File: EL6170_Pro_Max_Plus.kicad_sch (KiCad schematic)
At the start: 232 parts, among them CN1 PJ-327A0-SMT, J1 USB_C_Receptacle, J2 microSD, Q1 MMBT3904, Q2 MMBT3904, Q3 2N7002, Q4 AO3401A, Q5 AO3401A, SW1 SW_LEFT, SW10 SW_K4, SW11 SW_K5, SW12 SW_K6, SW13 SW_K7, SW14 SW_K8, SW15 SW_K9, SW16 SW_K0, SW17 SW_KQ, SW18 SW_KW, SW19 SW_KE, SW2 SW_UP, SW20 SW_KR, SW21 SW_KT, SW22 SW_KY, SW23 SW_KU, SW24 SW_KI, SW25 SW_KO, SW26 SW_KP, SW27 SW_KA, SW28 SW_KS, SW29 SW_KD, SW3 SW_DOWN, SW30 SW_KF, SW31 SW_KG, SW32 SW_KH, SW33 SW_KJ, SW34 SW_KK, SW35 SW_KL, SW36 SW_KZ, SW37 SW_KX, SW38 SW_KC, SW39 SW_KV, SW4 SW_RIGHT, SW40 SW_KB, SW41 SW_KN, SW42 SW_KM, SW43 SW_KCOM, SW44 SW_KDOT, SW45 SW_SHIFT, SW46 SW_CE(IO0), SW47 SW_OFF, SW48 SW_SECRET, SW49 SW_MCK, SW5 SW_UP2, SW50 SW_SPACE, SW51 SW_REMARK, SW52 SW_CALENDAR, SW53 SW_MODE, SW54 SW_ENTER, SW6 SW_DOWN2, SW7 SW_K1, SW8 SW_K2, SW9 SW_K3, U1 ESP32-S3, U10 ME6211C33M5, U11 TP5400_C2891434, U12 PCF8575DBR, U2 TPS61040DBV, U3 ESP-PSRAM64H, U4 W25Q128JVS, U5 ME6217C33M5, U6 CH340K, U7 RFANT5220110A0T, U8 CH334R, U9 PCM5102A, X1 40MHz, X2 12MHz

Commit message: PCB layout
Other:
- company: (none) -> libchara-dev
- title: (none) -> ProjectEL6170Pro
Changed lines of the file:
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@@
 	(generator_version "8.0")
 	(paper "A3")
+	(title_block
+		(title "ProjectEL6170Pro")
+		(date "2024-09-27")
+		(rev "2024-09-27")
+		(company "libchara-dev")
+		(comment 1 "EL6170 Pro Max Plus")
+	)
 	(junction
 		(at 245.11 199.39)

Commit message: sync
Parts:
- added R36: 10k, SparkFun-Resistor:R_0402_1005Metric, symbol SparkFun-Resistor:10k_0402
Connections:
- net STDBY is gone; now on net GPIO2: U11.4 (~{STDBY})
- net +3V3: now also R36.1
- net GPIO2: now also R36.2

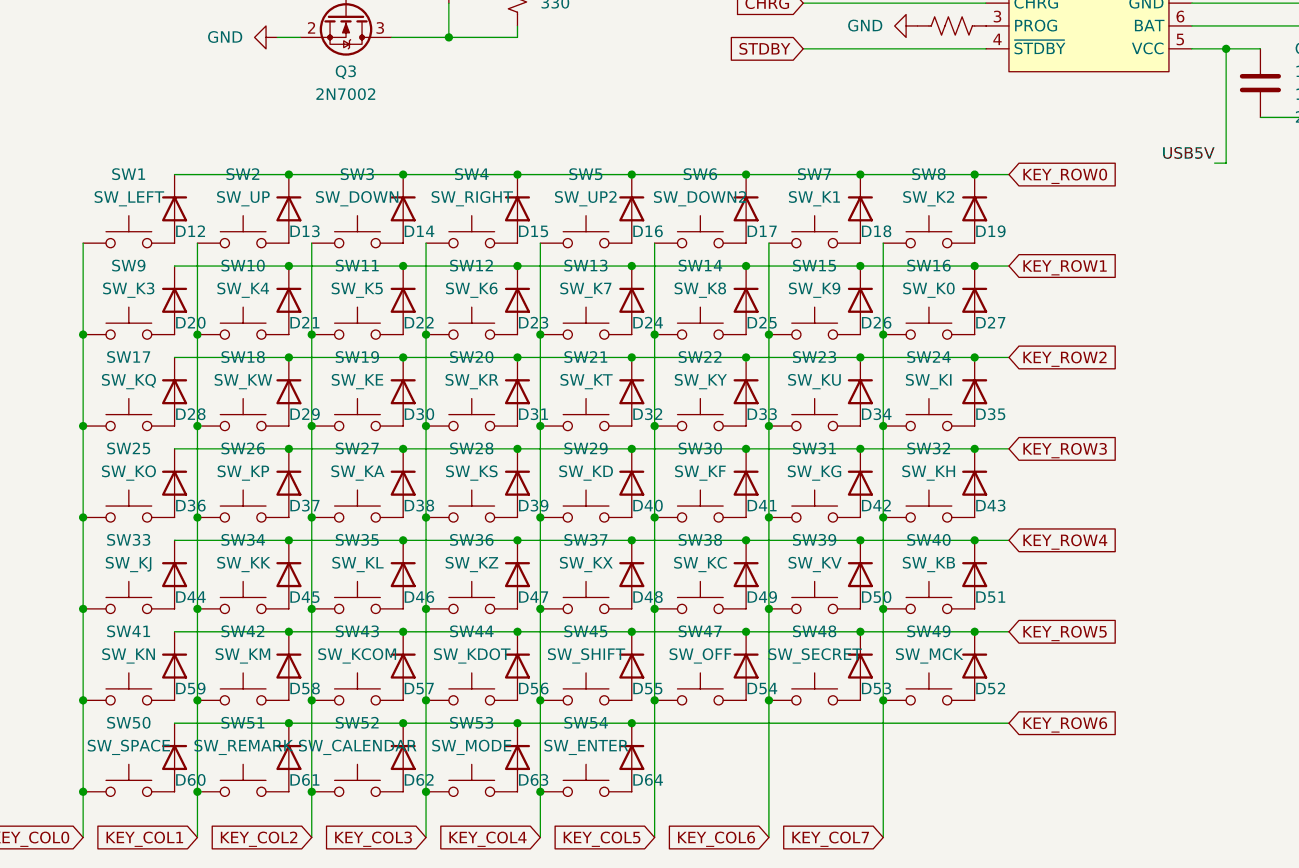
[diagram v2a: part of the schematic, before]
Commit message: Remove the diode from the keyboard
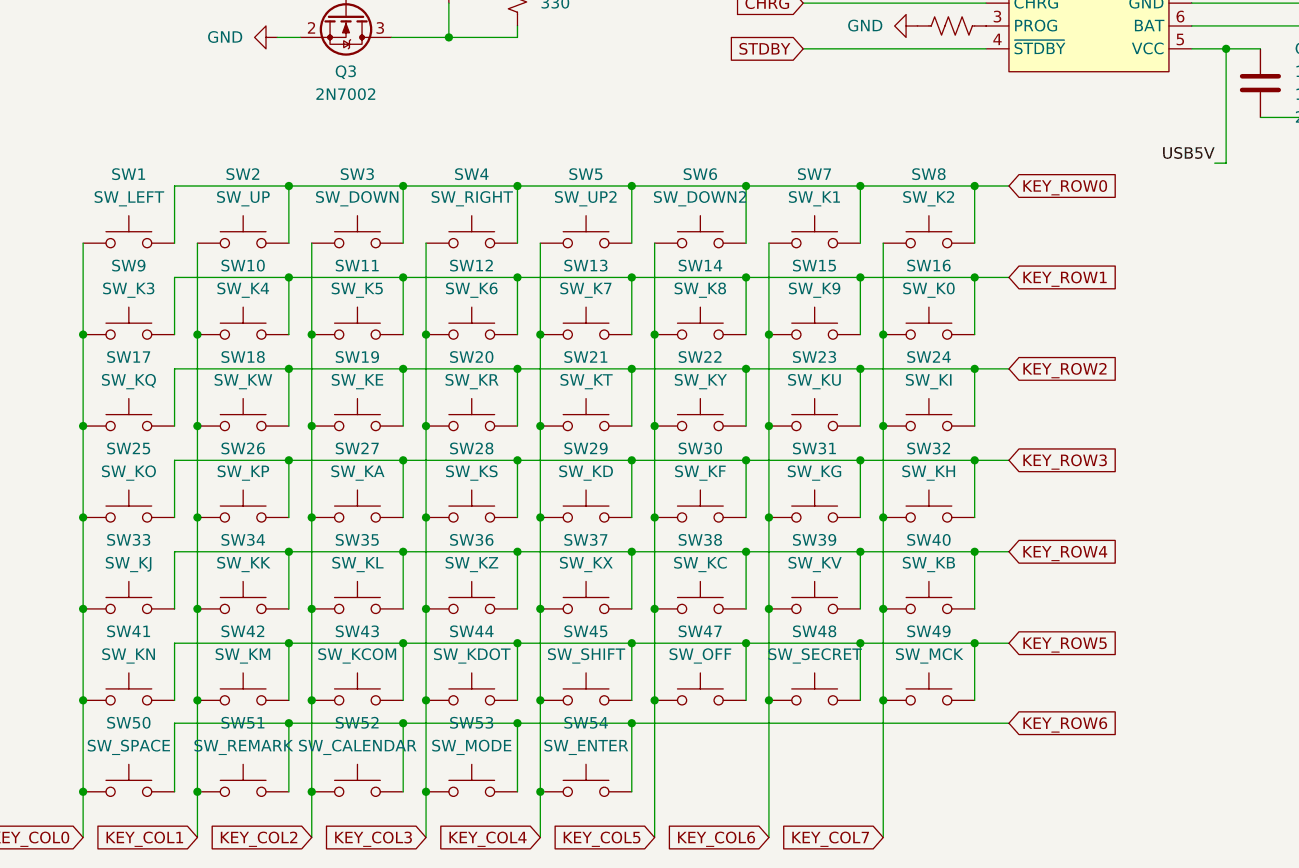
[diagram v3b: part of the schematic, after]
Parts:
- removed D12, D13, D14, D15, D16, D17, D18, D19, D20, D21, D22, D23, D24, D25, D26, D27, D28, D29, D30, D31, D32, D33, D34, D35, D36, D37, D38, D39, D40, D41, D42, D43, D44, D45, D46, D47, D48, D49, D50, D51, D52, D53, D54, D55, D56, D57, D58, D59, D60, D61, D62, D63, D64: 1N4148WS, Diode_SMD:D_SOD-323, symbol Diode:1N4148WS
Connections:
- net KEY_ROW0: now also SW1.2, SW2.2, SW3.2, SW4.2, SW5.2, SW6.2, SW7.2, SW8.2
- net KEY_ROW1: now also SW10.2, SW11.2, SW12.2, SW13.2, SW14.2, SW15.2, SW16.2, SW9.2
- net KEY_ROW2: now also SW17.2, SW18.2, SW19.2, SW20.2, SW21.2, SW22.2, SW23.2, SW24.2
- net KEY_ROW3: now also SW25.2, SW26.2, SW27.2, SW28.2, SW29.2, SW30.2, SW31.2, SW32.2
- net KEY_ROW4: now also SW33.2, SW34.2, SW35.2, SW36.2, SW37.2, SW38.2, SW39.2, SW40.2
- net KEY_ROW5: now also SW41.2, SW42.2, SW43.2, SW44.2, SW45.2, SW47.2, SW48.2, SW49.2
- net KEY_ROW6: now also SW50.2, SW51.2, SW52.2, SW53.2, SW54.2

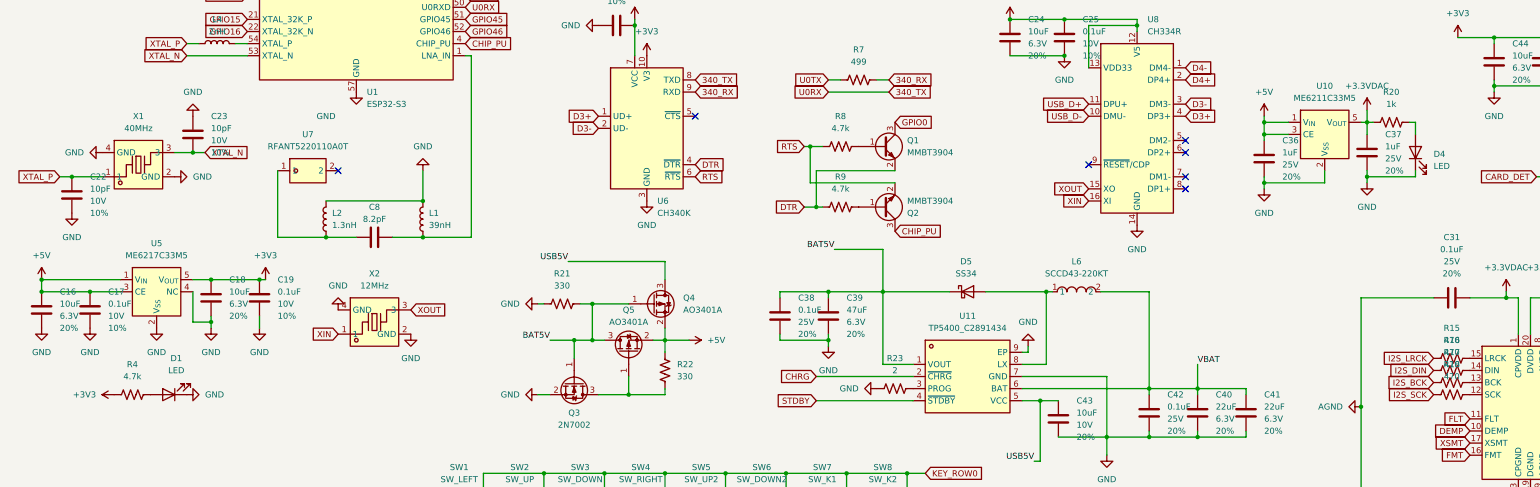
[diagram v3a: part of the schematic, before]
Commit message: Remove some LED
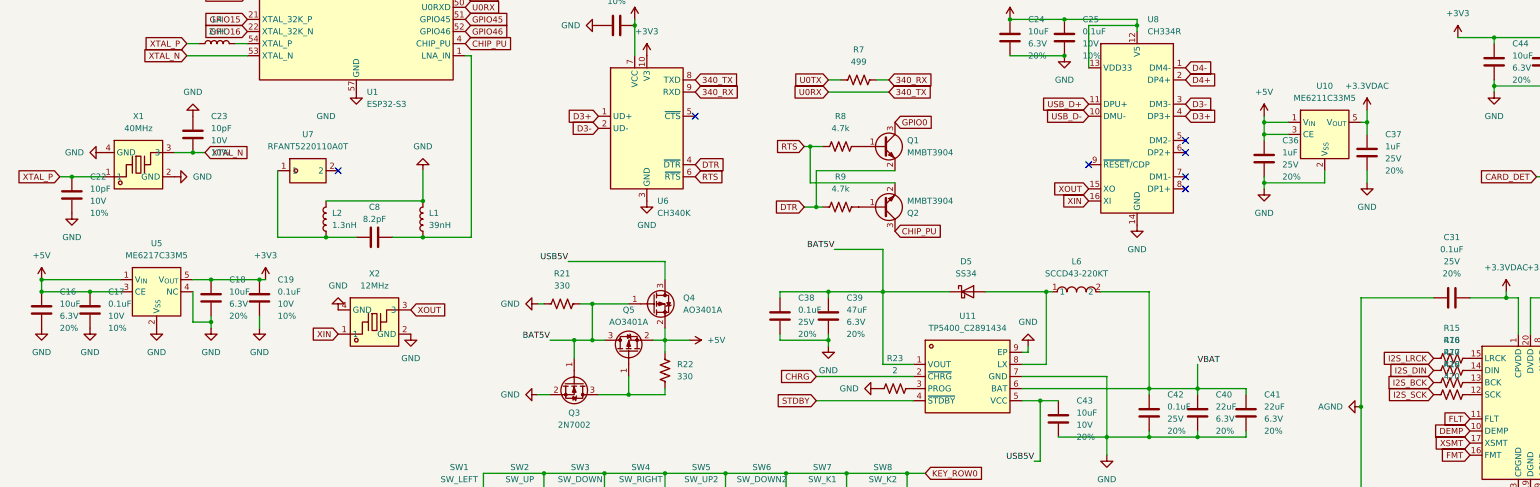
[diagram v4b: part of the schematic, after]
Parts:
- removed D1, D4: LED, SparkFun-LED:LED_0603_1608Metric, symbol SparkFun-LED:LED
- removed R20: 1k, SparkFun-Resistor:R_0603_1608Metric, symbol SparkFun-Resistor:1k_0603
- removed R4: 4.7k, SparkFun-Resistor:R_0402_1005Metric, symbol SparkFun-Resistor:4.7k_0402

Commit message: PCM5102A
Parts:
- removed CN1: PJ-327A0-SMT, easyeda2kicad:AUDIO-SMD_PJ-327A0-SMT, symbol easyeda2kicad:PJ-327A0-SMT
- added Audio1: PJ-320B, easyeda2kicad:AUDIO-SMD_PJ-320B, symbol easyeda2kicad:PJ-320B
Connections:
- net AGND: now also Audio1.1
- net LOUT: now also Audio1.3
- net ROUT: now also Audio1.2

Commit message: sync
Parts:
- removed C10: 1uF, SparkFun-Capacitor:C_0402_1005Metric, symbol SparkFun-Capacitor:0.1uF_0402_10V_10%
- removed C11: 10uF, SparkFun-Capacitor:C_0402_1005Metric, symbol SparkFun-Capacitor:10uF_0402_6.3V_20%
- removed C12, C13, C14, C15, C9: 0.1uF, SparkFun-Capacitor:C_0402_1005Metric, symbol SparkFun-Capacitor:0.1uF_0402_10V_10%
- removed C22, C23: 10pF, SparkFun-Capacitor:C_0603_1608Metric, symbol SparkFun-Capacitor:0.1uF_0402_10V_10%
- removed C8: 8.2pF, Capacitor_SMD:C_0402_1005Metric, symbol Device:C
- removed J1: USB_C_Receptacle, SparkFun-Connector:USB-C_16, symbol SparkFun-Connector:USB_C_Receptacle
- removed L1: 39nH, Inductor_SMD:L_0402_1005Metric, symbol Device:L
- removed L2: 1.3nH, Inductor_SMD:L_0402_1005Metric, symbol Device:L
- removed L3, L4: 2nH, Inductor_SMD:L_0402_1005Metric, symbol Device:L
- removed R2, R3: 5.1k, SparkFun-Resistor:R_0402_1005Metric, symbol SparkFun-Resistor:5.1k_0402
- removed U1: ESP32-S3, Package_DFN_QFN:QFN-56-1EP_7x7mm_P0.4mm_EP4x4mm, symbol MCU_Espressif:ESP32-S3
- removed U3: ESP-PSRAM64H, Package_SO:SOIC-8_3.9x4.9mm_P1.27mm, symbol Memory_RAM:ESP-PSRAM32
- removed U4: W25Q128JVS, Package_SO:SOIC-8_5.23x5.23mm_P1.27mm, symbol Memory_Flash:W25Q128JVS
- removed U7: RFANT5220110A0T, easyeda2kicad:FILTER-SMD_L5.2-W2.0-L, symbol easyeda2kicad:RFANT5220110A0T
- removed X1: 40MHz, easyeda2kicad:CRYSTAL-SMD_4P-L2.5-W2.0-BL, symbol easyeda2kicad:S2240000101050JY
- added C47, C48: 12pF, SparkFun-Capacitor:C_0402_1005Metric, symbol SparkFun-Capacitor:12pF_0402_50V_5%
- added C49: 0.1uF, SparkFun-Capacitor:C_0603_1608Metric, symbol SparkFun-Capacitor:0.1uF_0603_25V_20%
- added C50: 22uF, SparkFun-Capacitor:C_0603_1608Metric, symbol SparkFun-Capacitor:22uF_0603_6.3V_20%
- added R4: 0, SparkFun-Resistor:R_0402_1005Metric, symbol SparkFun-Resistor:0_0603
- added U13: ESP32-S3-WROOM-1U, RF_Module:ESP32-S3-WROOM-1U, symbol RF_Module:ESP32-S3-WROOM-1
- added USB1: MicroUSB, easyeda2kicad:MICRO-USB-SMD_MICRO-XNJ-ZB, symbol easyeda2kicad:MICROXNJZB
- added Y1: 32.768kHz, SparkFun-Clock:Crystal_SMD_3.2x1.5mm, symbol SparkFun-Clock:Crystal_32.768kHz_3.2x1.5mm
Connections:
- net +3V3: now also C49.1, C50.1, U13.2 (3V3)
- net 340_TX: now also U13.36 (RXD0)
- net AGND: now also R18.2, U9.10 (DEMP), U9.11 (FLT), U9.16 (FMT)
- net BAT_SMP: now also U13.18 (IO10)
- net CARD_DET: now also U13.11 (IO18)
- net CHIP_PU: now also U13.3 (EN)
- net D4+: now also U13.14 (IO20)
- net D4-: now also U13.13 (IO19)
- net GND: now also C47.1, C48.1, C49.2, C50.2, U13.1 (GND), U13.40 (GND), U13.41 (GND), USB1.5 (GND), USB1.6 (SHELL); no longer R18.2, U9.10 (DEMP), U9.11 (FLT), U9.16 (FMT)
- net GPIO0: now also U13.27 (IO0)
- net GPIO1: now also U13.39 (IO1)
- net GPIO11: now also U13.19 (IO11)
- net GPIO12: now also U13.20 (IO12)
- net GPIO13: now also U13.21 (IO13)
- net GPIO14: now also U13.22 (IO14)
- net GPIO17: now also U13.10 (IO17)
- net GPIO2: now also U13.38 (IO2)
- net GPIO21: now also U13.23 (IO21)
- net GPIO3: now also U13.15 (IO3)
- net GPIO35: now also U13.28 (IO35)
- net GPIO36: now also U13.29 (IO36)
- net GPIO37: now also U13.30 (IO37)
- net GPIO38: now also U13.31 (IO38)
- net GPIO39: now also U13.32 (IO39)
- net GPIO4: now also D9.2, J2.8 (DAT1), R29.2, U13.4 (IO4); no longer D11.2, J2.2 (DAT3/CD), R31.2
- net GPIO40: now also U13.33 (IO40)
- net GPIO41: now also U13.34 (IO41)
- net GPIO42: now also U13.35 (IO42)
- net GPIO45: now also U13.26 (IO45)
- net GPIO46: now also U13.16 (IO46)
- net GPIO47: now also U13.24 (IO47)
- net GPIO48: now also U13.25 (IO48)
- net GPIO5: now also D8.2, J2.7 (DAT0/SDO), R28.2, U13.5 (IO5); no longer D10.2, J2.1 (DAT2), R30.2
- net GPIO6: now also D7.2, J2.5 (CLK/SCK), R27.2, U13.6 (IO6); no longer D9.2, J2.8 (DAT1), R29.2
- net GPIO7: now also D6.2, J2.3 (CMD/SDI), R26.2, U13.7 (IO7); no longer D8.2, J2.7 (DAT0/SDO), R28.2
- net GPIO8: now also D11.2, J2.2 (DAT3/CD), R31.2, U13.12 (IO8); no longer D7.2, J2.5 (CLK/SCK), R27.2
- net GPIO9: now also D10.2, J2.1 (DAT2), R30.2, U13.17 (IO9); no longer D6.2, J2.3 (CMD/SDI), R26.2
- net U0TX: now also U13.37 (TXD0)
- net USB5V: now also USB1.1 (VBUS)
- net USB_D+: now also USB1.3 (D+)
- net USB_D-: now also USB1.2 (D-)
- new net: C47.2, R4.1, U13.8 (IO15), Y1.1
- new net: C48.2, R4.2, U13.9 (IO16), Y1.2
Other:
- moved on the sheet: D2, R10, R36
